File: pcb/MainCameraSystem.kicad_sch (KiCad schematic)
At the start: 0 parts

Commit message: Added STM32H533VET6 and connector for OV5640.
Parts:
- added J1: OV5640 Ribbon Connector, pcb:Flat Flexible Cable 24-Pin 0.5mm Connector, symbol Connector:Conn_01x24_Pin
- added U1: STM32H533VET6, Package_QFP:LQFP-100_14x14mm_P0.5mm, symbol MCU_ST_STM32H5:STM32H533VETx
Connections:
- new net +3.3V: U1.100 (VDD), U1.11 (VDD), U1.22 (VDDA), U1.28 (VDD), U1.50 (VDD), U1.75 (VDD)
- new net GND: U1.10 (VSS), U1.19 (VSSA), U1.27 (VSS), U1.49 (VSS), U1.74 (VSS), U1.99 (VSS)
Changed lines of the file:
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@@
 	(generator "eeschema")
 	(generator_version "9.0")
-	(paper "A4")
-	(sheet_instances
-		(path "/"
-			(page "1")
-		)
-	)
-	(embedded_fonts no)
-)
+	(paper "A2")

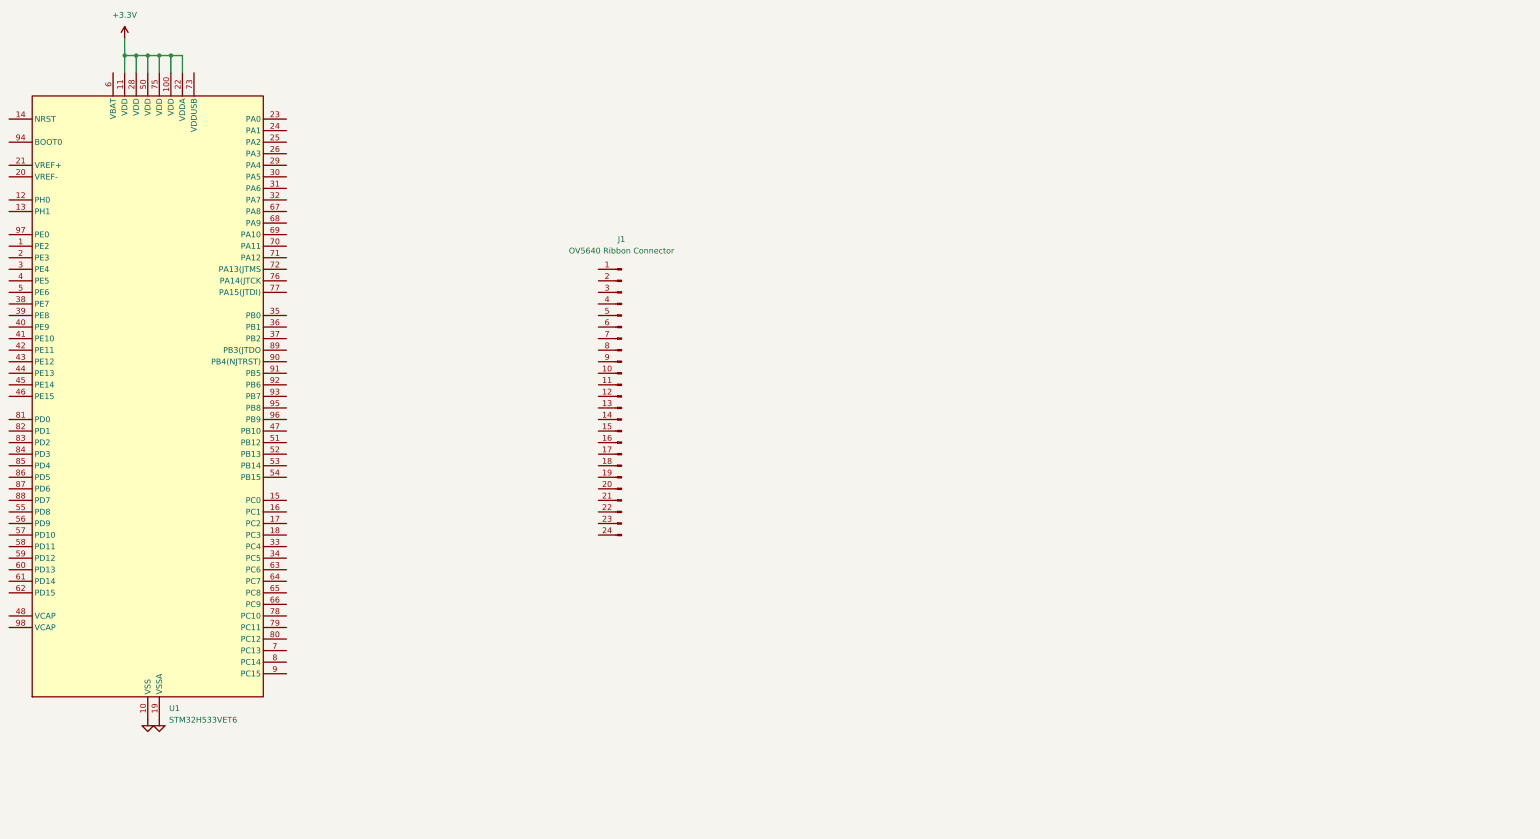
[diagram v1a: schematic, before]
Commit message: Labeled pins for the FFC connector.
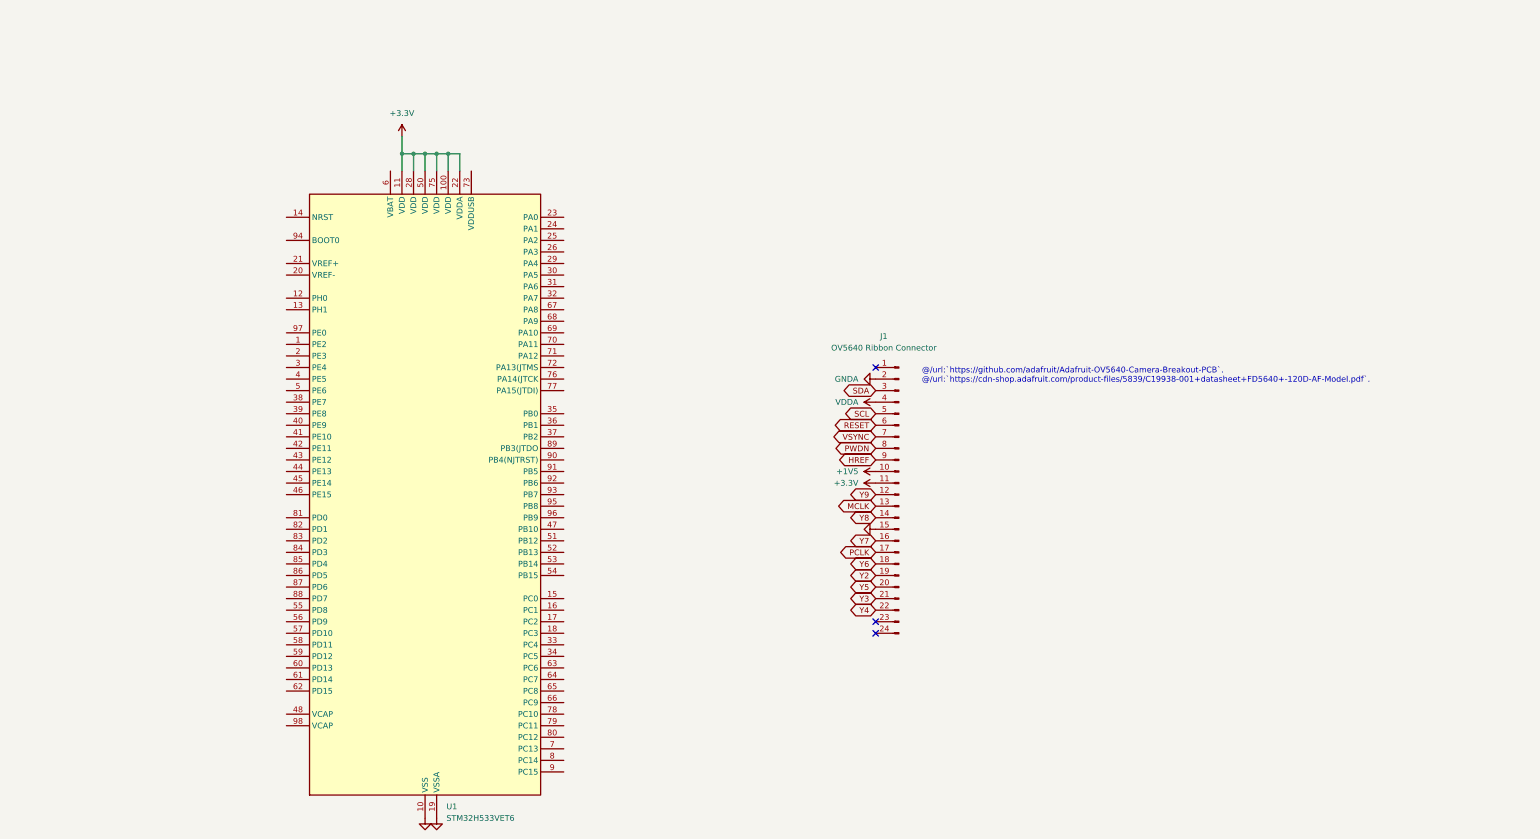
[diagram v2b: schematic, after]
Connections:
- net +3.3V: now also J1.11 (Pin_11)
- net GND: now also J1.15 (Pin_15)
- net +1V5: now reaches J1.10 (Pin_10)
- net Y9: now reaches J1.12 (Pin_12)
- net MCLK: now reaches J1.13 (Pin_13)
- net Y8: now reaches J1.14 (Pin_14)
- net Y7: now reaches J1.16 (Pin_16)
- net PCLK: now reaches J1.17 (Pin_17)
- net Y6: now reaches J1.18 (Pin_18)
- net Y2: now reaches J1.19 (Pin_19)
- net GNDA: now reaches J1.2 (Pin_2)
- net Y5: now reaches J1.20 (Pin_20)
- net Y3: now reaches J1.21 (Pin_21)
- net Y4: now reaches J1.22 (Pin_22)
- net SDA: now reaches J1.3 (Pin_3)
- net VDDA: now reaches J1.4 (Pin_4)
- net SCL: now reaches J1.5 (Pin_5)
- net RESET: now reaches J1.6 (Pin_6)
- net VSYNC: now reaches J1.7 (Pin_7)
- net PWDN: now reaches J1.8 (Pin_8)
- net HREF: now reaches J1.9 (Pin_9)
- no-connect marks 0 -> 3
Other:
- note added: "@/url:`https://github.com/adafruit/Adafruit-OV5640-Camera-Breakout-PCB`. @/url:`https://cdn-shop.adafruit.com/product-files/5839/C19938-001+datasheet+FD5640+-120D-AF-Model.pdf`."
- moved on the sheet: J1, U1

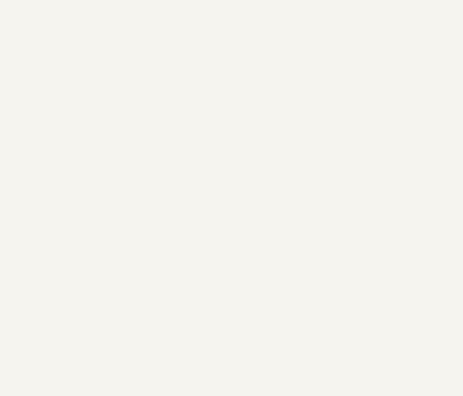
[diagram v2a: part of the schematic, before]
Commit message: Added electronics box as reference housing.
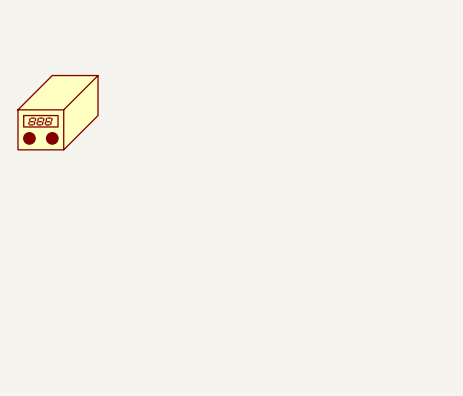
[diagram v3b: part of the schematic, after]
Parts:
- added N1: Housing, pcb:MainCameraSystemHousing, symbol Mechanical:Housing

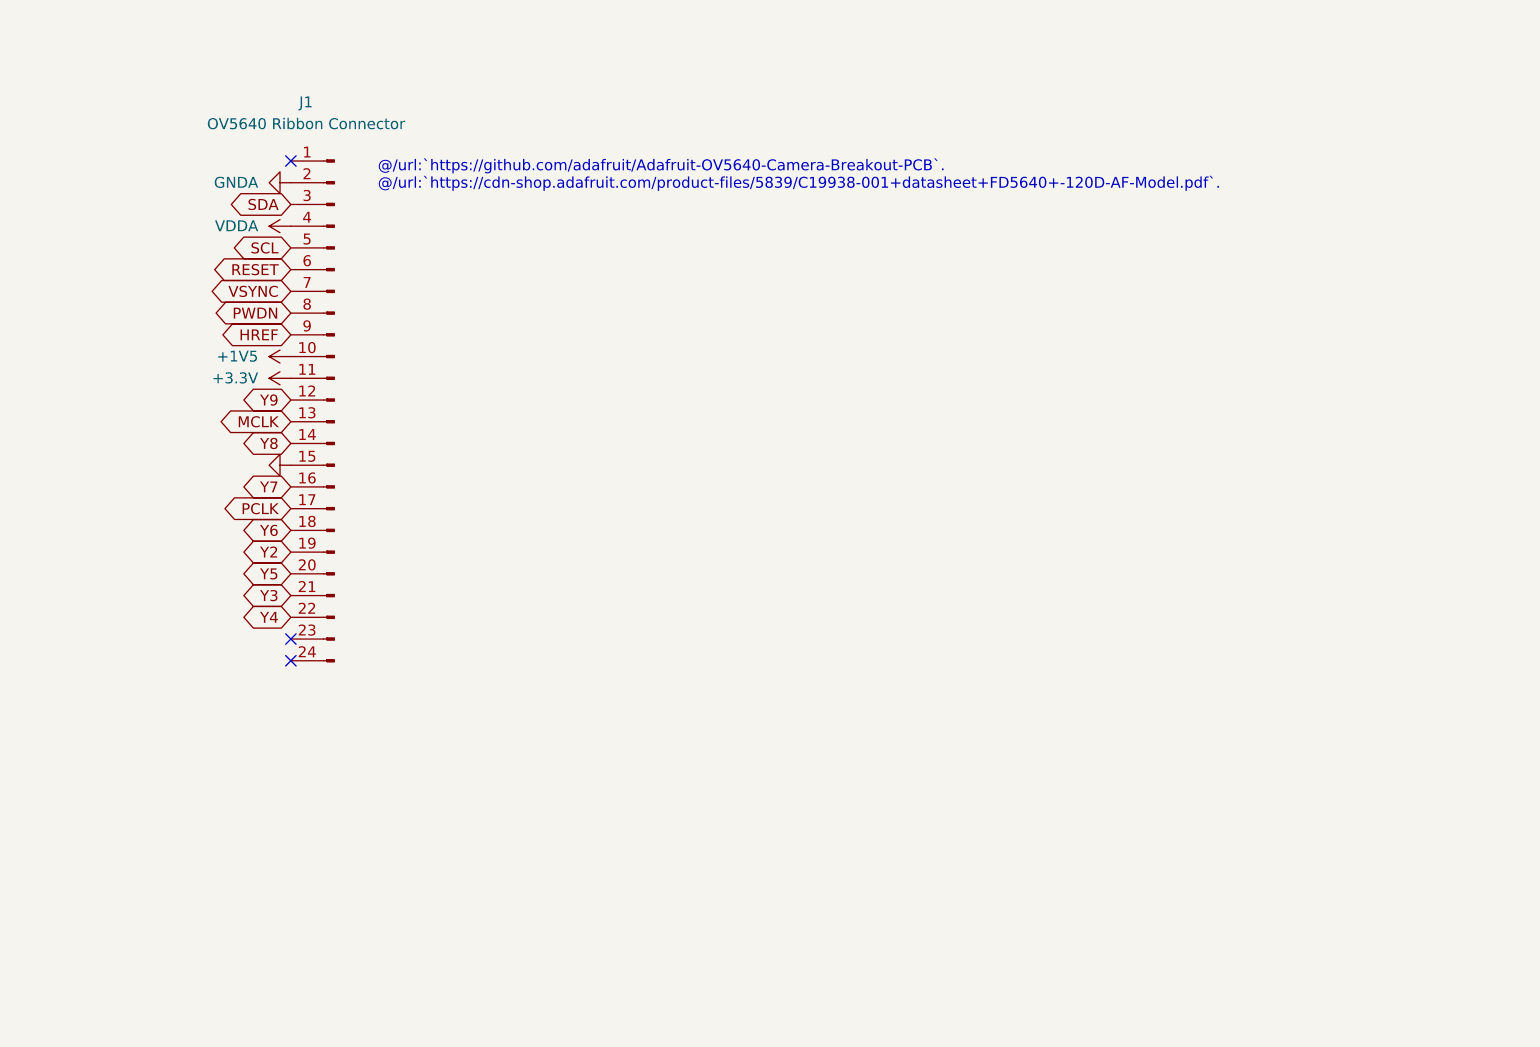
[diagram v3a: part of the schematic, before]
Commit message: Added connector for ST-Link.
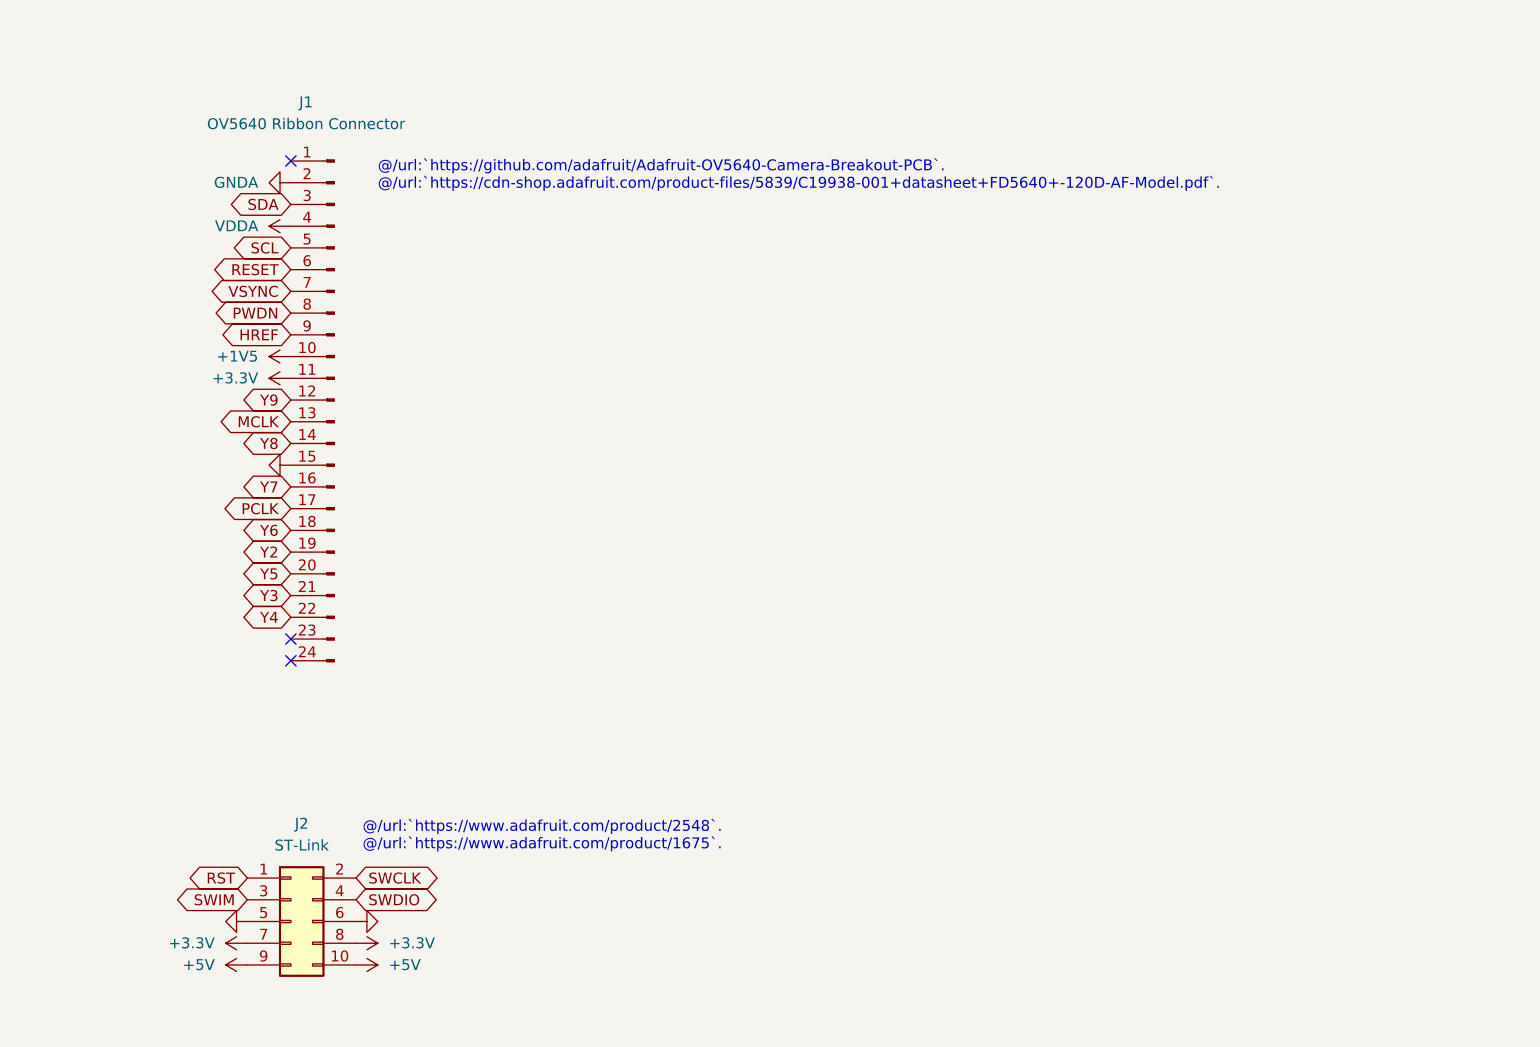
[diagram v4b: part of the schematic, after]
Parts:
- added J2: ST-Link, Connector_IDC:IDC-Header_2x05_P2.54mm_Horizontal, symbol Connector_Generic:Conn_02x05_Odd_Even
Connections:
- net +3.3V: now also J2.7 (Pin_7), J2.8 (Pin_8)
- net GND: now also J2.5 (Pin_5), J2.6 (Pin_6)
- new net +5V: J2.10 (Pin_10), J2.9 (Pin_9)
- new net RST: J2.1 (Pin_1)
- new net SWCLK: J2.2 (Pin_2)
- new net SWDIO: J2.4 (Pin_4)
- new net SWIM: J2.3 (Pin_3)
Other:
- note added: "@/url:`https://www.adafruit.com/product/2548`. @/url:`https://www.adafruit.com/product/1675`."

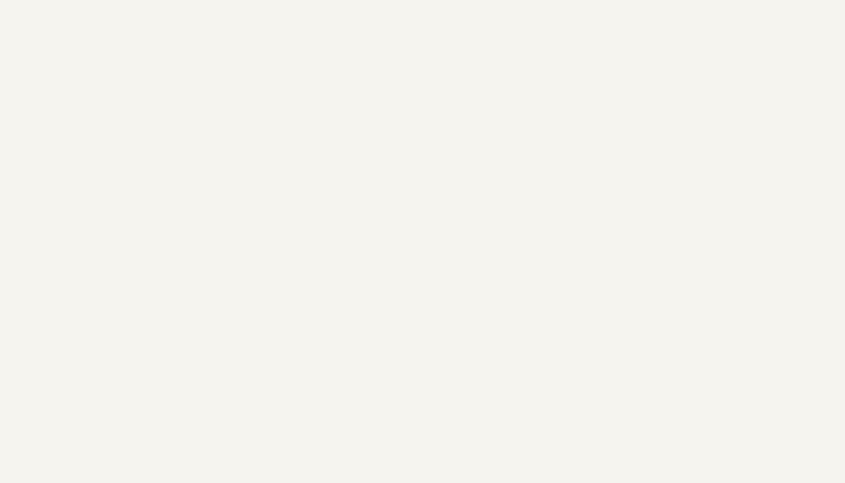
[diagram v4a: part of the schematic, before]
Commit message: Added uSD connector.
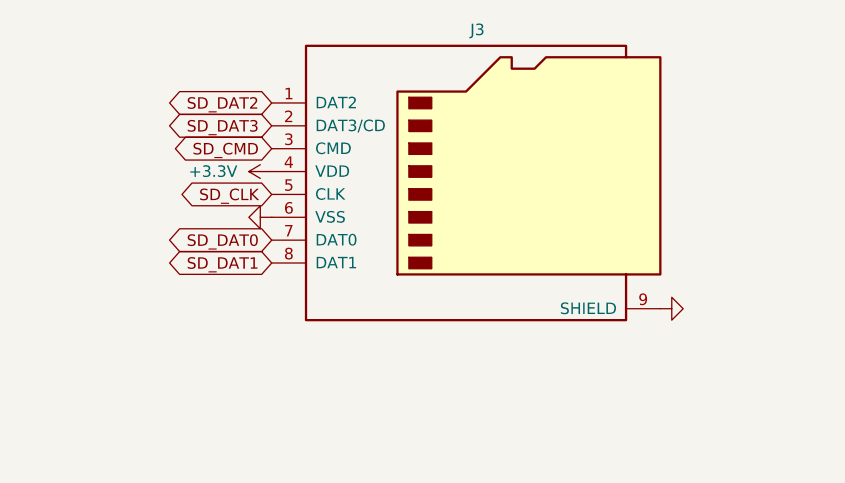
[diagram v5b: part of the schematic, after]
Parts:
- added J3: Micro_SD_Card, pcb:microSD_HC_Molex_47219-2001, symbol Connector:Micro_SD_Card
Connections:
- net +3.3V: now also J3.4 (VDD)
- net GND: now also J3.6 (VSS), J3.9 (SHIELD)
- new net SD_CLK: J3.5 (CLK)
- new net SD_CMD: J3.3 (CMD)
- new net SD_DAT0: J3.7 (DAT0)
- new net SD_DAT1: J3.8 (DAT1)
- new net SD_DAT2: J3.1 (DAT2)
- new net SD_DAT3: J3.2 (DAT3/CD)

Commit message: Ported MCP changes.
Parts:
- added D1: GREEN, LED_SMD:LED_1206_3216Metric_Pad1.42x1.75mm_HandSolder, symbol Device:LED
- added D2: RED, LED_SMD:LED_1206_3216Metric_Pad1.42x1.75mm_HandSolder, symbol Device:LED
- added J4: USB_B_Micro, Connector_USB:USB_Micro-B_Molex-105017-0001, symbol Connector:USB_B_Micro
- added R1, R2: 2K, Resistor_SMD:R_1206_3216Metric_Pad1.30x1.75mm_HandSolder, symbol Device:R
- added U2: MCP2221AxST, Package_SO:TSSOP-14_4.4x5mm_P0.65mm, symbol Interface_USB:MCP2221AxST
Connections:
- net +3.3V: now also U2.1 (VDD), U2.11 (VUSB)
- net GND: now also D1.1 (K), D2.1 (K), J4.5 (GND), J4.6 (Shield), U2.14 (VSS)
- new net: J4.2 (D-), U2.12 (D-)
- new net: J4.3 (D+), U2.13 (D+)
- new net: D1.2 (A), R1.1
- new net: R1.2, U2.2 (GP0)
- new net: D2.2 (A), R2.2
- new net: R2.1, U2.3 (GP1)
- new net SERIAL_RESET: U2.4 (~{RST})
- new net SERIAL_RX: U2.5 (URx)
- new net SERIAL_TX: U2.6 (UTx)
- no-connect marks 3 -> 8
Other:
- note added: "@/pg 3/tbl l-1/`MCP2221A`."

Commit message: Integrated UART Bridge onto Camera PCB
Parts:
- J4: footprint Connector_USB:USB_Micro-B_Molex-105017-0001 -> Connector_USB:USB_Micro-B_Molex_47346-0001

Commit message: Emptied out schematic and layout of `MainCameraSystem`.
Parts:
- removed D1: GREEN, LED_SMD:LED_1206_3216Metric_Pad1.42x1.75mm_HandSolder, symbol Device:LED
- removed D2: RED, LED_SMD:LED_1206_3216Metric_Pad1.42x1.75mm_HandSolder, symbol Device:LED
- removed J1: OV5640 Ribbon Connector, pcb:Flat Flexible Cable 24-Pin 0.5mm Connector, symbol Connector:Conn_01x24_Pin
- removed J2: ST-Link, Connector_IDC:IDC-Header_2x05_P2.54mm_Horizontal, symbol Connector_Generic:Conn_02x05_Odd_Even
- removed J3: Micro_SD_Card, pcb:microSD_HC_Molex_47219-2001, symbol Connector:Micro_SD_Card
- removed J4: USB_B_Micro, Connector_USB:USB_Micro-B_Molex_47346-0001, symbol Connector:USB_B_Micro
- removed N1: Housing, pcb:MainCameraSystemHousing, symbol Mechanical:Housing
- removed R1, R2: 2K, Resistor_SMD:R_1206_3216Metric_Pad1.30x1.75mm_HandSolder, symbol Device:R
- removed U1: STM32H533VET6, Package_QFP:LQFP-100_14x14mm_P0.5mm, symbol MCU_ST_STM32H5:STM32H533VETx
- removed U2: MCP2221AxST, Package_SO:TSSOP-14_4.4x5mm_P0.65mm, symbol Interface_USB:MCP2221AxST
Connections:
- no-connect marks 8 -> 0
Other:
- note removed: "@/pg 3/tbl l-1/`MCP2221A`."
- note removed: "@/url:`https://github.com/adafruit/Adafruit-OV5640-Camera-Breakout-PCB`. @/url:`https://cdn-shop.adafruit.com/product-files/5839/C19938-001+datasheet+FD5640+-120D-AF-Model.pdf`."
- note removed: "@/url:`https://www.adafruit.com/product/2548`. @/url:`https://www.adafruit.com/product/1675`."
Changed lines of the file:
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@@
 	(generator_version "9.0")
 	(paper "A2")
+	(sheet_instances
+		(path "/"
+			(page "1")
+		)
+	)
+	(embedded_fonts no)
+	(embedded_files
+		(file
+			(name "sheet.kicad_wks")
+			(type worksheet)
+			(data |KLUv/SDtTQQA8kcaGHDNA0DI0YHeJkZJsFFVHWPECK8T+nf7Ruut19T/Wjj1lcRtZEY9sbORjzTz
+				BIaRKX941NSZJ0BmPfl9qd8ptZzn+0ZINNlsfT9aMk5jtv60TTtxar2BmQMgAoxWv7Yhp9ZdInlM
+				wxcXCyAQIoF8eJTajUPCXqolYFHFD/FgziWduMYHggI=|
+			)
+			(checksum "00BCE598336E5951A5D0C187D2E96FE2")
+		)
+	)
+)
